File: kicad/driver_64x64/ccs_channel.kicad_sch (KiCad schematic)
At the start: 4 parts

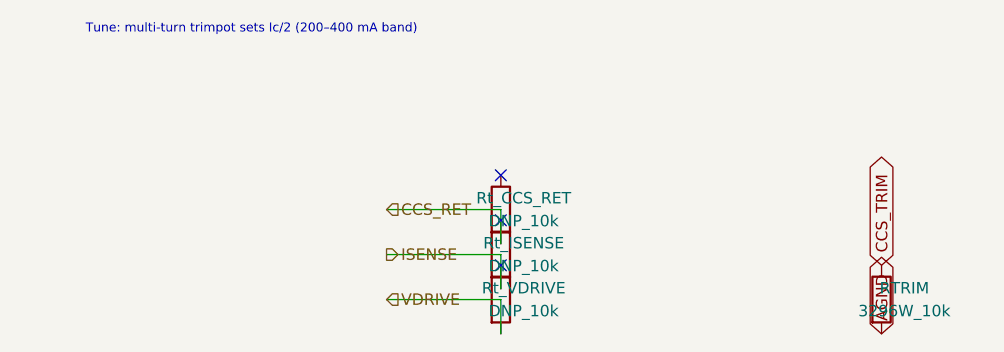
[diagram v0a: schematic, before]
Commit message: logical seperation into host and multiple decode/drive/steering boards
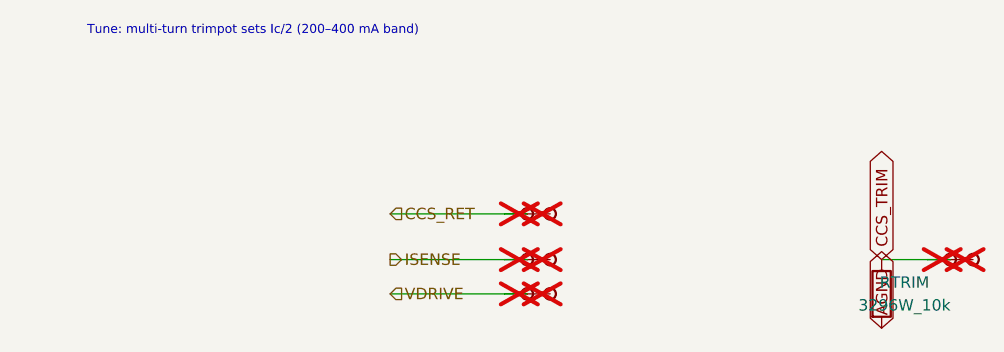
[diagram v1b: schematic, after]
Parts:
- removed Rt_CCS_RET, Rt_ISENSE, Rt_VDRIVE: DNP_10k, symbol Device:R
- added TP_CCS_RET, TP_CCS_RETb, TP_CCS_TRIM_80_01_35_, TP_CCS_TRIM_80_01_35_b, TP_ISENSE, TP_ISENSEb, TP_VDRIVE, TP_VDRIVEb: Stub, symbol CMR:Stub
- RTRIM: symbol Device:R -> CMR:R
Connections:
- net CCS_RET: now also TP_CCS_RET.1, TP_CCS_RETb.1
- net CCS_TRIM: now also TP_CCS_TRIM_80_01_35_.1, TP_CCS_TRIM_80_01_35_b.1
- net ISENSE: now also TP_ISENSE.1, TP_ISENSEb.1
- net VDRIVE: now also TP_VDRIVE.1, TP_VDRIVEb.1
- no-connect marks 3 -> 0
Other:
- moved on the sheet: RTRIM
